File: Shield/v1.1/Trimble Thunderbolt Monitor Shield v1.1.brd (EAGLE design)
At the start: 60.9 x 54.3 mm, 32 parts, among them Q1 2N2222, U1 MAX232PTH

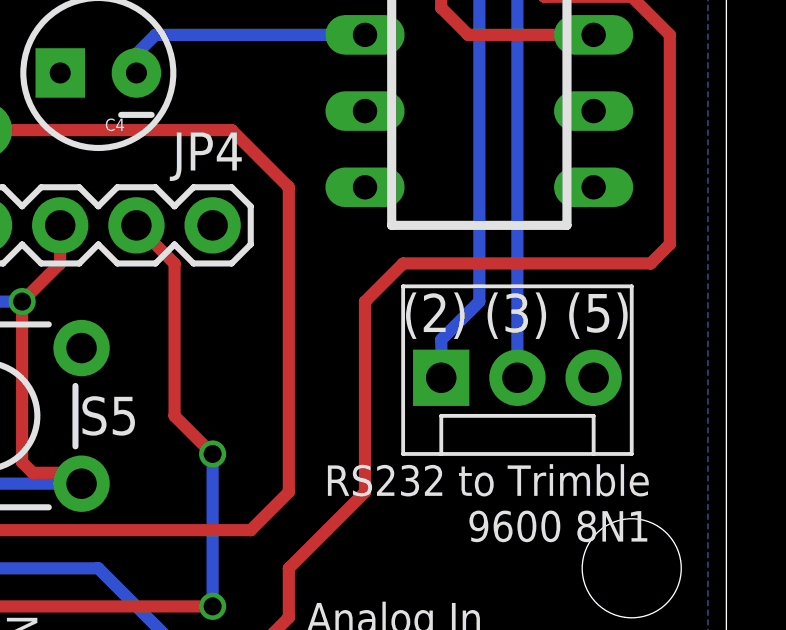
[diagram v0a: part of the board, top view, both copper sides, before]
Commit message: Fixed some silkscreen issues
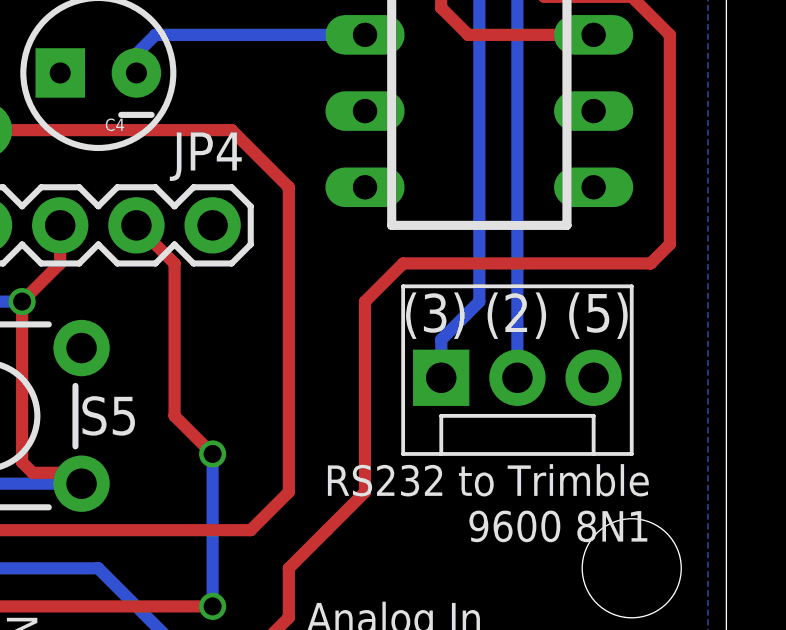
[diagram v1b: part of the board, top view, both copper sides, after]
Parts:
- S1: value RIGHT -> (none)
- S2: value UP -> (none)
- S3: value DOWN -> (none)
- S4: value LEFT -> (none)
- S5: value SELECT -> (none)
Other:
- board text added: "(3) (2) (5)"
- board text removed: "(2) (3) (5)"
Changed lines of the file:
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@@
 <text x="40.64" y="42.545" size="1.016" layer="21" rot="R180">RST</text>
 <text x="24.892" y="78.867" size="1.27" layer="21" rot="R270">Contrast</text>
-<text x="80.01" y="56.134" size="1.27" layer="21" rot="R180">(2) (3) (5)</text>
+<text x="80.01" y="56.134" size="1.27" layer="21" rot="R180">(3) (2) (5)</text>
 <text x="62.865" y="78.105" size="1.4224" layer="21" rot="R180">V1.1</text>
 </plain>
@@
 <element name="JP1" library="pinhead" package="1X16" value="HD44780" x="45.72" y="83.82"/>
 <element name="U1" library="SparkFun" package="DIL16" value="MAX232PTH" x="74.93" y="68.58" rot="R270"/>
-<element name="S2" library="SparkFun" package="TACTILE-PTH" value="UP" x="29.21" y="52.07" smashed="yes">
+<element name="S2" library="SparkFun" package="TACTILE-PTH" value="" x="29.21" y="52.07" smashed="yes">
 <attribute name="NAME" x="32.385" y="51.435" size="1.27" layer="25" ratio="10"/>
 </element>
-<element name="S3" library="SparkFun" package="TACTILE-PTH" value="DOWN" x="29.21" y="44.45" smashed="yes">
+<element name="S3" library="SparkFun" package="TACTILE-PTH" value="" x="29.21" y="44.45" smashed="yes">
 <attribute name="NAME" x="32.385" y="43.815" size="1.27" layer="25" ratio="10"/>
 </element>
-<element name="S4" library="SparkFun" package="TACTILE-PTH" value="LEFT" x="39.37" y="52.07" smashed="yes">
+<element name="S4" library="SparkFun" package="TACTILE-PTH" value="" x="39.37" y="52.07" smashed="yes">
 <attribute name="NAME" x="42.545" y="51.435" size="1.27" layer="25" ratio="10"/>
 </element>
-<element name="S5" library="SparkFun" package="TACTILE-PTH" value="SELECT" x="58.42" y="52.07" smashed="yes">
+<element name="S5" library="SparkFun" package="TACTILE-PTH" value="" x="58.42" y="52.07" smashed="yes">
 <attribute name="NAME" x="61.595" y="51.435" size="1.27" layer="25" ratio="10"/>
 </element>
@@
 <element name="C3" library="SparkFun" package="CPOL-RADIAL-10UF-25V" value="1uF" x="74.93" y="82.55" rot="R180"/>
 <element name="C4" library="SparkFun" package="CPOL-RADIAL-10UF-25V" value="1uF" x="62.23" y="63.5" rot="R180"/>
-<element name="S1" library="SparkFun" package="TACTILE-PTH" value="RIGHT" x="49.53" y="52.07" smashed="yes">
+<element name="S1" library="SparkFun" package="TACTILE-PTH" value="" x="49.53" y="52.07" smashed="yes">
 <attribute name="NAME" x="52.705" y="51.435" size="1.27" layer="25" ratio="10"/>
 </element>

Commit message: Subtle cleanup of the v1.1 board and gerber files
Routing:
- net N$20: track 48.4 -> 46.9 mm
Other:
- board text added: "Thunderbolt Monitor"
- board text removed: "Trimble Thunderbolt Monitor"
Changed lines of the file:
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@@
 <layer number="26" name="bNames" color="7" fill="1" visible="yes" active="yes"/>
 <layer number="27" name="tValues" color="7" fill="1" visible="yes" active="yes"/>
-<layer number="28" name="bValues" color="7" fill="1" visible="no" active="yes"/>
+<layer number="28" name="bValues" color="7" fill="1" visible="yes" active="yes"/>
 <layer number="29" name="tStop" color="7" fill="3" visible="no" active="yes"/>
 <layer number="30" name="bStop" color="7" fill="6" visible="no" active="yes"/>
@@
 <wire x1="83.165" y1="93.015" x2="22.225" y2="93.015" width="0" layer="20"/>
 <wire x1="22.225" y1="93.015" x2="22.225" y2="38.735" width="0" layer="20"/>
-<text x="71.12" y="81.28" size="1.016" layer="21" rot="R180">Trimble Thunderbolt Monitor</text>
-<text x="54.61" y="78.74" size="1.016" layer="21">http://www.m1dst.co.uk</text>
+<text x="69.85" y="81.915" size="1.27" layer="21" rot="R180">Thunderbolt Monitor</text>
+<text x="53.34" y="78.74" size="1.27" layer="21">http://www.m1dst.co.uk</text>
 <text x="58.42" y="74.295" size="1.6764" layer="22" font="vector" rot="MR0">http://www.m1dst.co.uk</text>
 <text x="80.645" y="50.419" size="1.016" layer="21" rot="R180">RS232 to Trimble
@@
 <wire x1="25.9588" y1="49.8094" x2="32.4612" y2="49.8094" width="0.4064" layer="16"/>
 <wire x1="36.83" y1="61.595" x2="39.37" y2="61.595" width="0.4064" layer="1"/>
-<wire x1="32.4612" y1="49.8094" x2="32.4612" y2="49.53" width="0.4064" layer="1"/>
-<wire x1="32.4612" y1="49.53" x2="31.115" y2="49.53" width="0.4064" layer="1"/>
-<wire x1="31.115" y1="49.53" x2="30.48" y2="50.165" width="0.4064" layer="1"/>
-<wire x1="36.83" y1="61.595" x2="31.115" y2="61.595" width="0.4064" layer="1"/>
-<wire x1="31.115" y1="61.595" x2="30.48" y2="60.96" width="0.4064" layer="1"/>
-<wire x1="30.48" y1="60.96" x2="30.48" y2="50.165" width="0.4064" layer="1"/>
 <contactref element="JP4" pad="2"/>
 <wire x1="39.37" y1="61.595" x2="42.545" y2="61.595" width="0.4064" layer="1"/>
@@
 <wire x1="52.07" y1="63.5" x2="53.34" y2="62.23" width="0.4064" layer="1"/>
 <wire x1="53.34" y1="62.23" x2="53.34" y2="58.42" width="0.4064" layer="1"/>
+<wire x1="36.83" y1="61.595" x2="32.385" y2="61.595" width="0.4064" layer="1"/>
+<wire x1="32.385" y1="61.595" x2="31.75" y2="60.96" width="0.4064" layer="1"/>
+<wire x1="31.75" y1="60.96" x2="31.75" y2="57.15" width="0.4064" layer="1"/>
+<wire x1="31.75" y1="57.15" x2="30.48" y2="55.88" width="0.4064" layer="1"/>
+<wire x1="30.48" y1="55.88" x2="30.48" y2="50.8" width="0.4064" layer="1"/>
+<wire x1="30.48" y1="50.8" x2="31.4706" y2="49.8094" width="0.4064" layer="1"/>
+<wire x1="31.4706" y1="49.8094" x2="32.4612" y2="49.8094" width="0.4064" layer="1"/>
 </signal>
 <signal name="D13">
